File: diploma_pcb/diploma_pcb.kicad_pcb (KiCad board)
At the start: 2 copper layers, 50 x 24 mm, 21 parts, among them Q1 2SC3356, Q3 2SC3356

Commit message: fixed PCB/Word
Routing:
- net GND: track 96.1 -> 98.6 mm
- net green: track 11.0 -> 10.3 mm

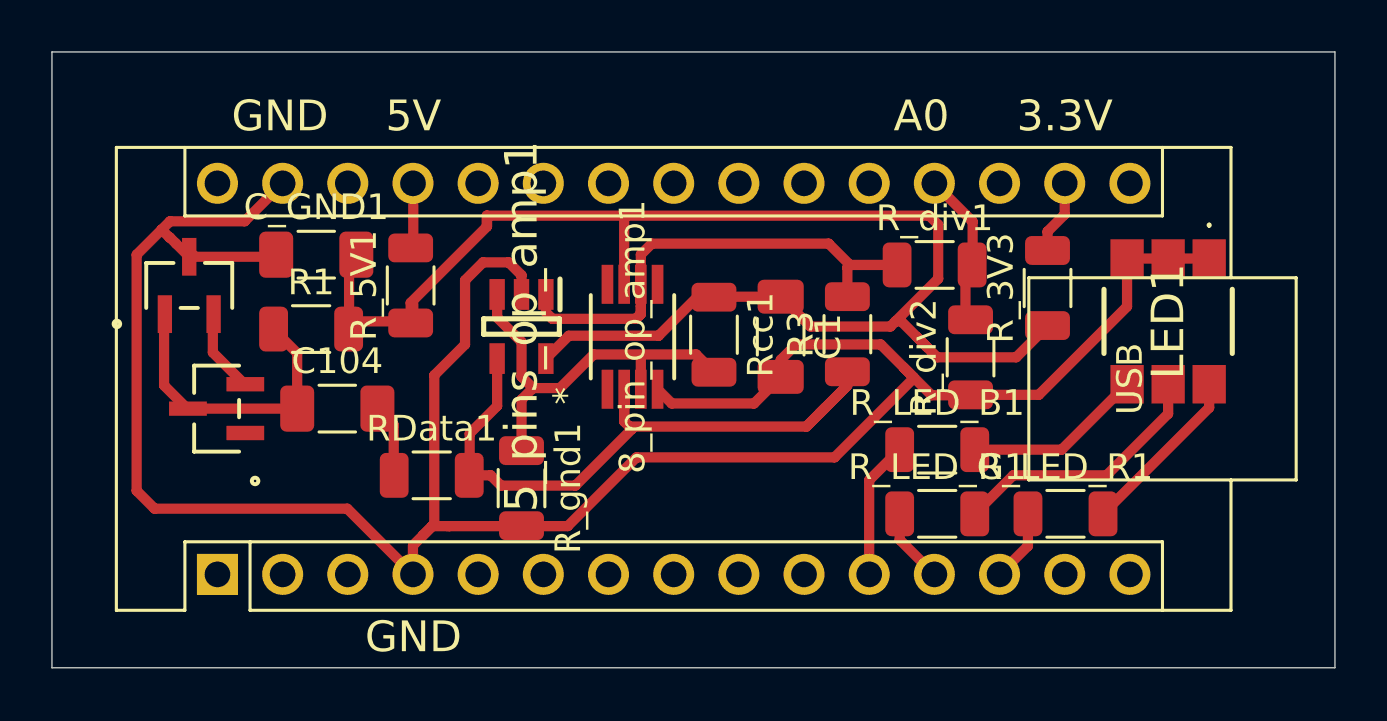
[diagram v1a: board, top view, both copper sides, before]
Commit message: PCB added cap, larger pads, partialy fixed footprints
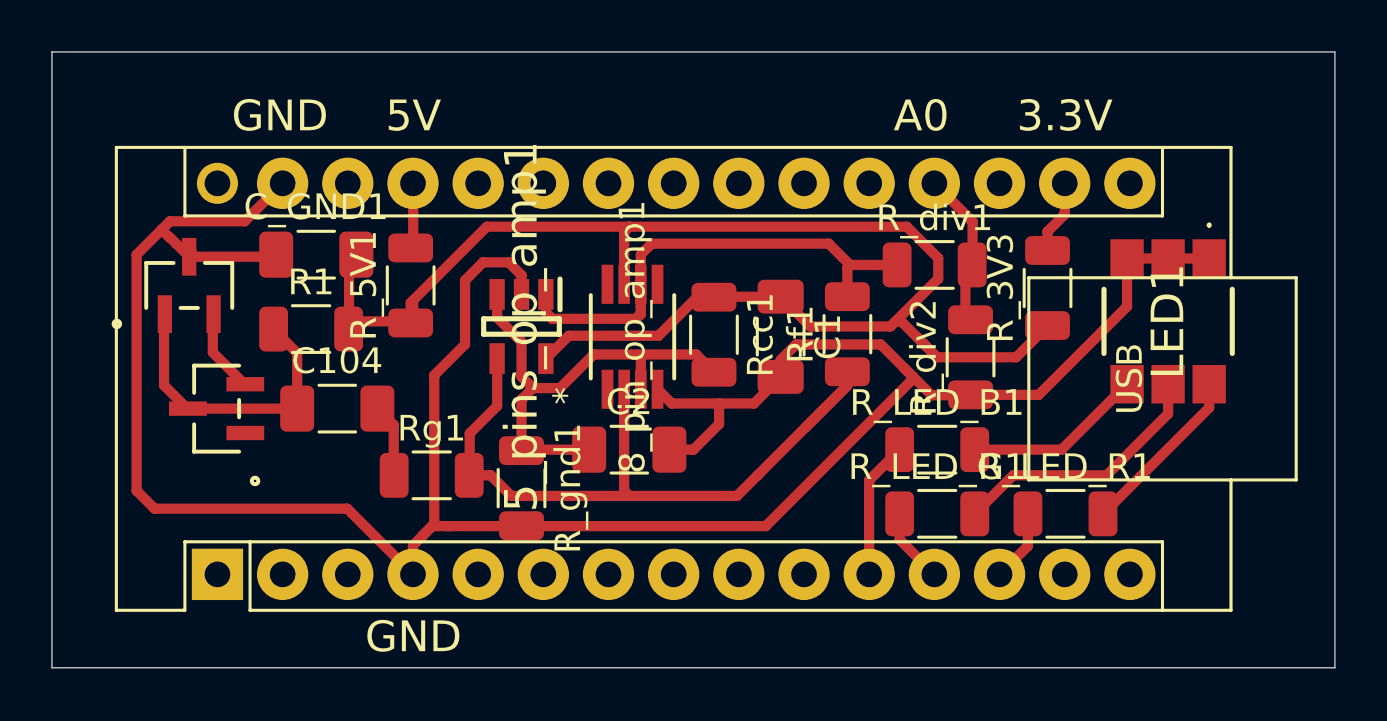
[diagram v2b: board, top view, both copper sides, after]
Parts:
- added C2: .1uF, Capacitor_SMD:C_1206_3216Metric_Pad1.33x1.80mm_HandSolder, F.Cu at (48.5, 65.0)
- R1: value R -> 2k
- R_gnd1, Rcc1: value R -> 3k
- Rf1: renamed from R3; value R -> 510к
- Rg1: renamed from RData1; value R -> 15к
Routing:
- net GND: track 98.6 -> 101.8 mm
- net signal: track 27.5 -> 30.2 mm
- net non inv: track 15.9 -> 18.6 mm
- net Supply: track 60.2 -> 58.1 mm

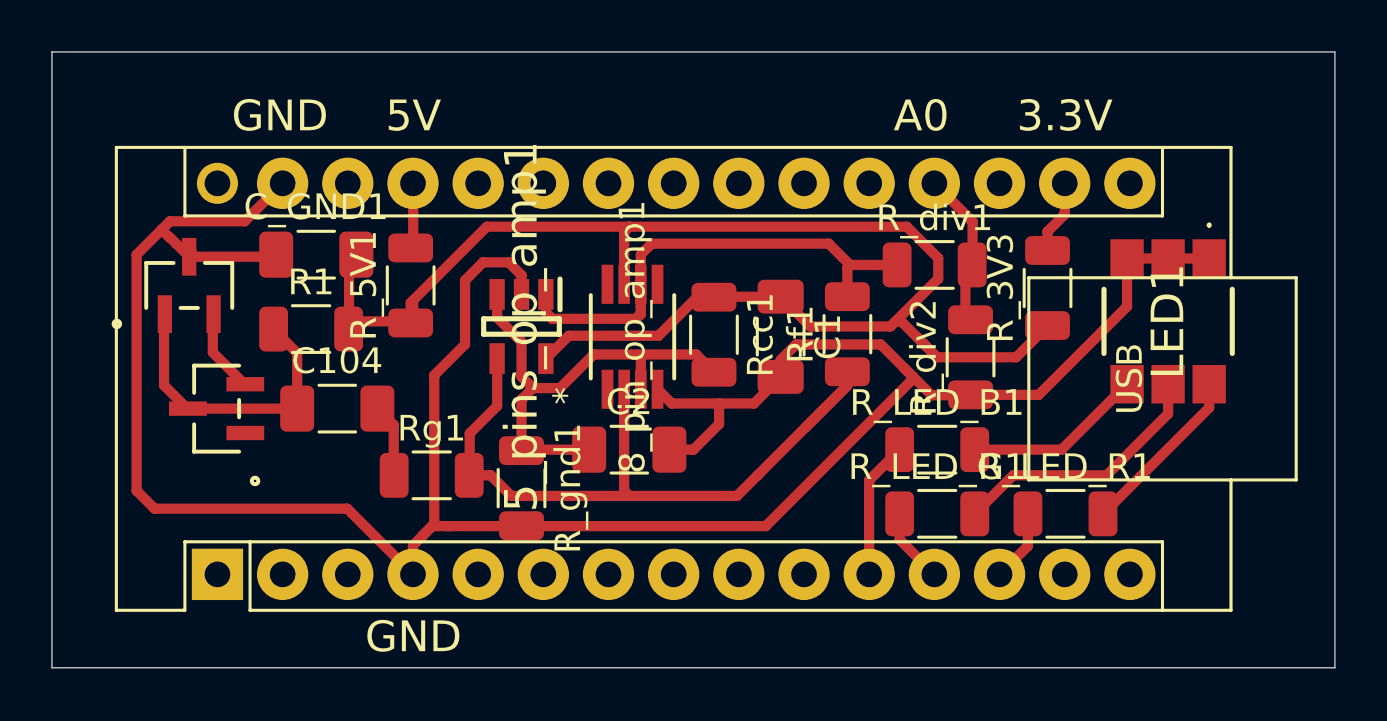
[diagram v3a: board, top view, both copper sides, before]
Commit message: Daemon created, Footprint Assigned, Device constatnly sending
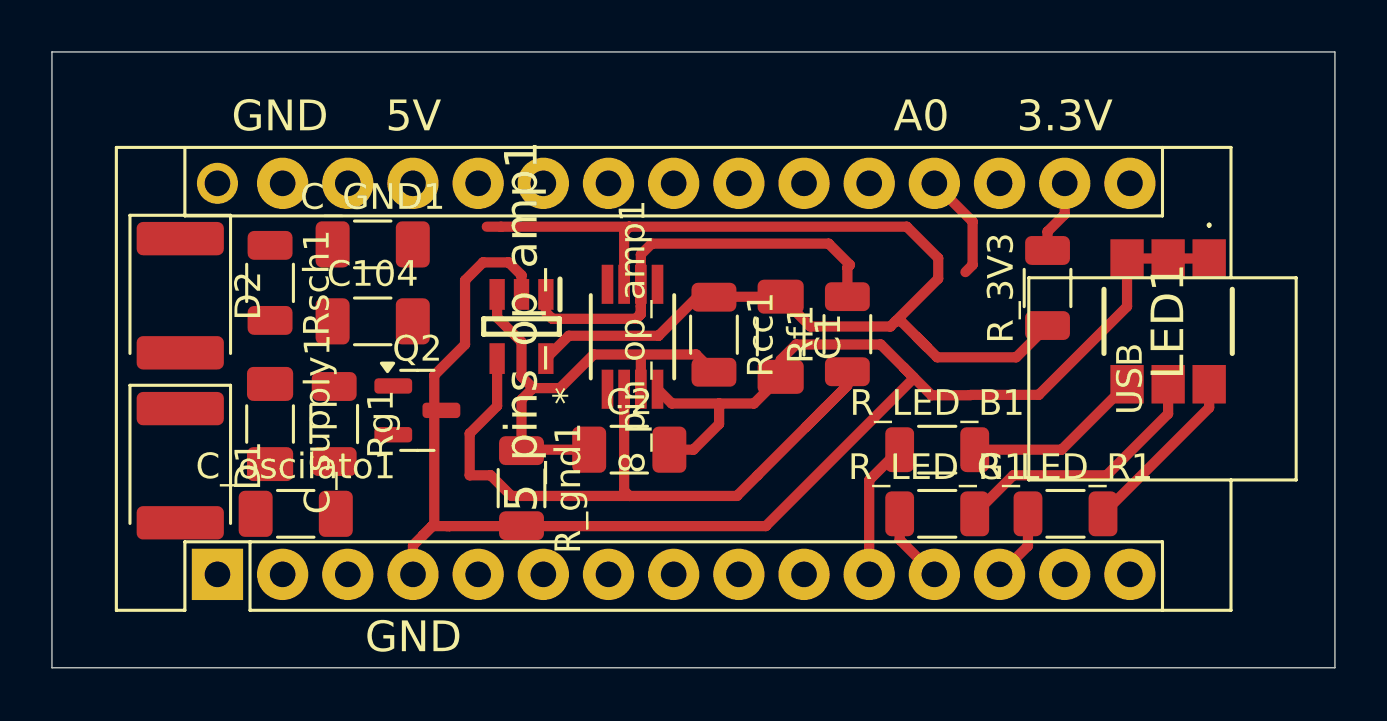
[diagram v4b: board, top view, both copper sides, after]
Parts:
- removed Q1, Q3: 2SC3356, 2SC3356:SOT-23_MINIMOLD_REN
- removed R1: 2k, Resistor_SMD:R_1206_3216Metric
- removed R_5V1, R_div1, R_div2: R, Resistor_SMD:R_1206_3216Metric
- added C_oscilato1: .1uF, Capacitor_SMD:C_1206_3216Metric_Pad1.33x1.80mm_HandSolder, F.Cu at (35.5, 67.5)
- added C_supply1: .1uF, Capacitor_SMD:C_1206_3216Metric_Pad1.33x1.80mm_HandSolder, F.Cu at (34.5, 64.0)
- added D1: D_Schottky, Diode_SMD:D_1812_4532Metric_Pad1.30x3.40mm_HandSolder, F.Cu at (31.0, 65.6)
- added D2: D_Schottky, Diode_SMD:D_1812_4532Metric_Pad1.30x3.40mm_HandSolder, F.Cu at (31.0, 59.0)
- added Q2: 2n3904, Package_TO_SOT_SMD:SOT-23, F.Cu at (40.2, 63.5)
- added Rsch1: 1M, Resistor_SMD:R_1206_3216Metric, F.Cu at (34.5, 58.5)
- R_LED_B1, R_LED_G1, R_LED_R1: value R -> 220
- R_gnd1, Rcc1: value 3k -> 4.7k
- Rf1: value 510к -> 680k
- Rg1: value 15к -> 10k
- moved Rg1 4.29 mm to (37.0, 64.0), turned to -90 degrees
- moved C104 3.67 mm to (38.5, 60.0)
- moved C_GND1 2.24 mm to (38.5, 57.0)
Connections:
- net signal renamed Signal
- 5_pins_op_amp1 pad 5: Supply -> 5V
- 8_pin_op_amp1 pad 7: Supply -> 5V
- A1 pad 17: 3.3V -> unconnected-(A1-3V3-Pad17)
- A1 pad 19: Net-(A1-A0) -> Vout
- A1 pad 6: unconnected-(A1-D3-Pad6) -> Net-(A1-D3)
- C1 pad 1: Supply -> 5V
- C_GND1 pad 2: Supply -> 5V
- Rcc1 pad 1: Supply -> 5V
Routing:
- net GND: track 101.8 -> 68.4 mm
- net Net-(Q2-E): track 11.7 -> 0.00 mm
- net Supply: track 58.1 -> 47.0 mm
- net Net-(A1-A0): track 6.03 -> 0.00 mm
- net Net-(Q1-B): track 3.04 -> 0.00 mm
- net Net-(C104-Pad2): track 2.86 -> 0.00 mm
- net Vout: track 19.1 -> 21.5 mm
- net 5V: track 1.67 -> 0.00 mm

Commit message: PCB created (not checked), ard changes?, Footprints set up
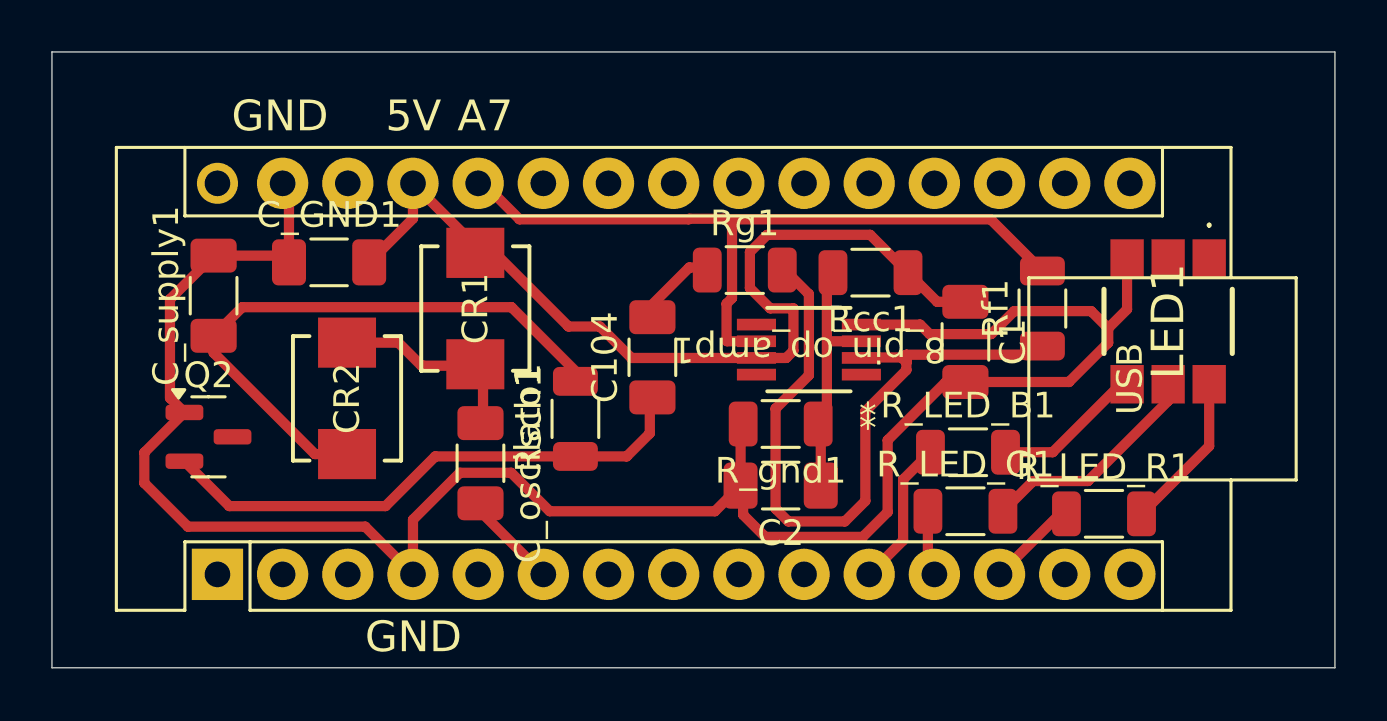
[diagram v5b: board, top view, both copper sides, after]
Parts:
- removed 5_pins_op_amp1: MCP6291T-E_OT, op_amp_MCP6291T-E/OT:SOT95P280X145-5N
- removed D1, D2: D_Schottky, Diode_SMD:D_1812_4532Metric_Pad1.30x3.40mm_HandSolder
- removed R_3V3: R, Resistor_SMD:R_1206_3216Metric
- added CR1: MBRS1100T3G, MBRS1100T3G:SMB_403A-03_ONS, F.Cu at (42.5, 59.5)
- added CR2: MBRS1100T3G, MBRS1100T3G:SMB_403A-03_ONS, F.Cu at (37.5, 63.0)
- moved Rg1 17.1 mm to (53.0, 58.0), turned to 0 degrees
- moved Rsch1 13.0 mm to (46.4, 63.8), turned to 90 degrees
- moved C104 11.0 mm to (49.4, 61.4), turned to 90 degrees
- moved R_gnd1 10.4 mm to (54.4, 64.0), turned to 180 degrees
- moved Q2 8.21 mm to (32.1, 64.5)
- moved Rf1 7.67 mm to (64.6, 59.5)
- moved C_oscilato1 7.47 mm to (42.7, 65.5), turned to -90 degrees
- moved C1 7.20 mm to (61.6, 60.8)
- moved 8_pin_op_amp1 6.89 mm to (55.5, 61.1), turned to 180 degrees
- moved Rcc1 6.56 mm to (57.9, 58.1), turned to 180 degrees
- moved C2 6.06 mm to (54.4, 66.4), turned to 180 degrees
- moved C_supply1 5.46 mm to (32.3, 59.0), turned to 90 degrees
- moved C_GND1 1.84 mm to (36.8, 57.7)
- moved R_LED_R1 1.50 mm to (67.0, 67.5)
- moved R_LED_B1 1.20 mm to (61.7, 65.1)
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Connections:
- A1 pad 19: Vout -> unconnected-(A1-A0-Pad19)
- A1 pad 26: unconnected-(A1-A7-Pad26) -> Vout
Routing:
- net Supply: track 47.0 -> 0.00 mm
- net 5V: track 0.00 -> 36.7 mm
- net Net-(CR2-Pad1): track 0.00 -> 23.7 mm
- net Net-(Q2-E): track 0.00 -> 21.4 mm
- net GND: track 68.4 -> 82.2 mm
- net non inv: track 18.6 -> 9.72 mm
- net Net-(CR1-Pad1): track 0.00 -> 8.03 mm
- net Vout: track 21.5 -> 29.4 mm
- net Net-(A1-D3): track 0.00 -> 3.78 mm
- net 3.3V: track 2.88 -> 0.00 mm
- net Net-(C104-Pad2): track 0.00 -> 2.73 mm
- net Signal: track 30.2 -> 27.9 mm
- net green: track 10.3 -> 8.87 mm
- net red: track 7.33 -> 6.14 mm
- net blue: track 6.99 -> 5.84 mm
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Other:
- board text added: "A7"
- board text removed: "3.3V"
- board text removed: "A0"

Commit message: driver communicating and functioning successfully
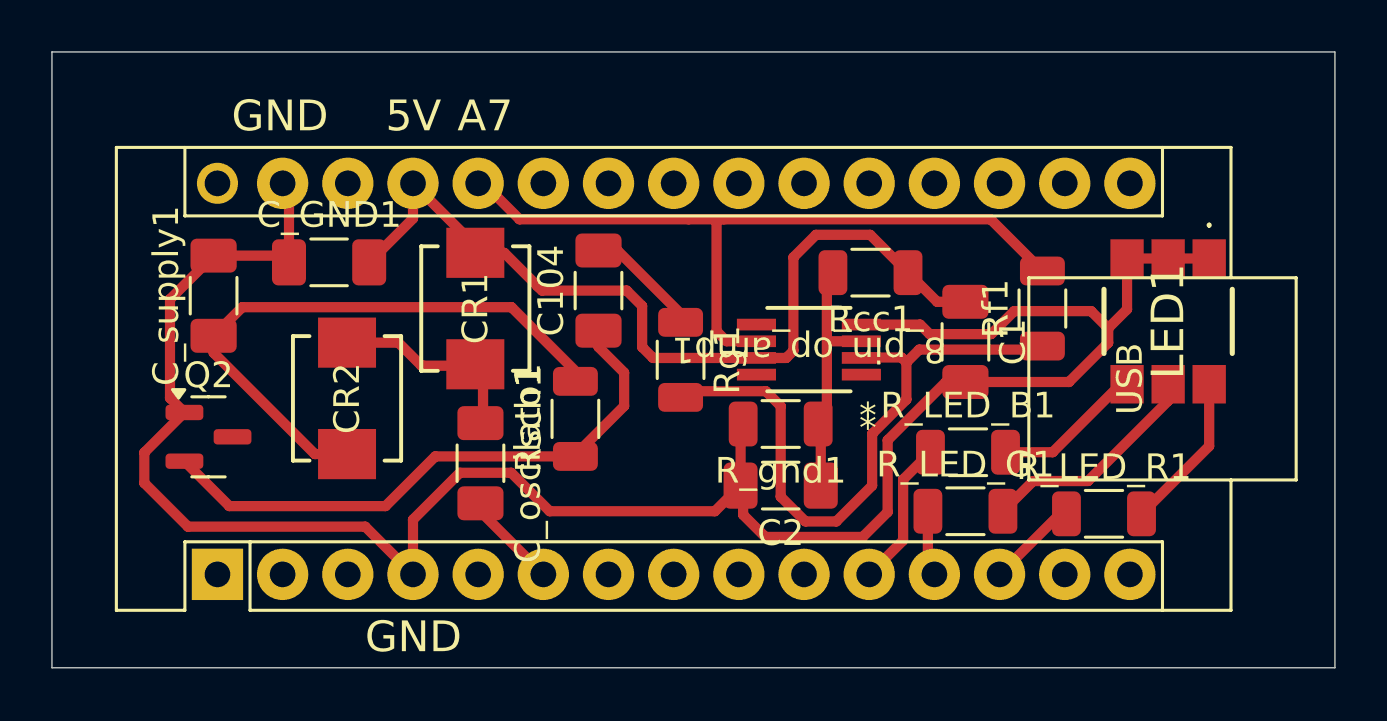
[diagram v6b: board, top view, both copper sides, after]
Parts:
- moved Rg1 4.30 mm to (50.5, 61.5), turned to -90 degrees
- moved C104 3.34 mm to (47.3, 58.8)
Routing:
- net Signal: track 27.9 -> 24.3 mm
- net GND: track 82.2 -> 85.4 mm
- net Net-(C104-Pad2): track 2.73 -> 4.70 mm
- net Net-(Q2-E): track 21.4 -> 22.8 mm
- net 5V: track 36.7 -> 35.5 mm
